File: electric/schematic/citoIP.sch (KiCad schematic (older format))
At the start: 31 parts

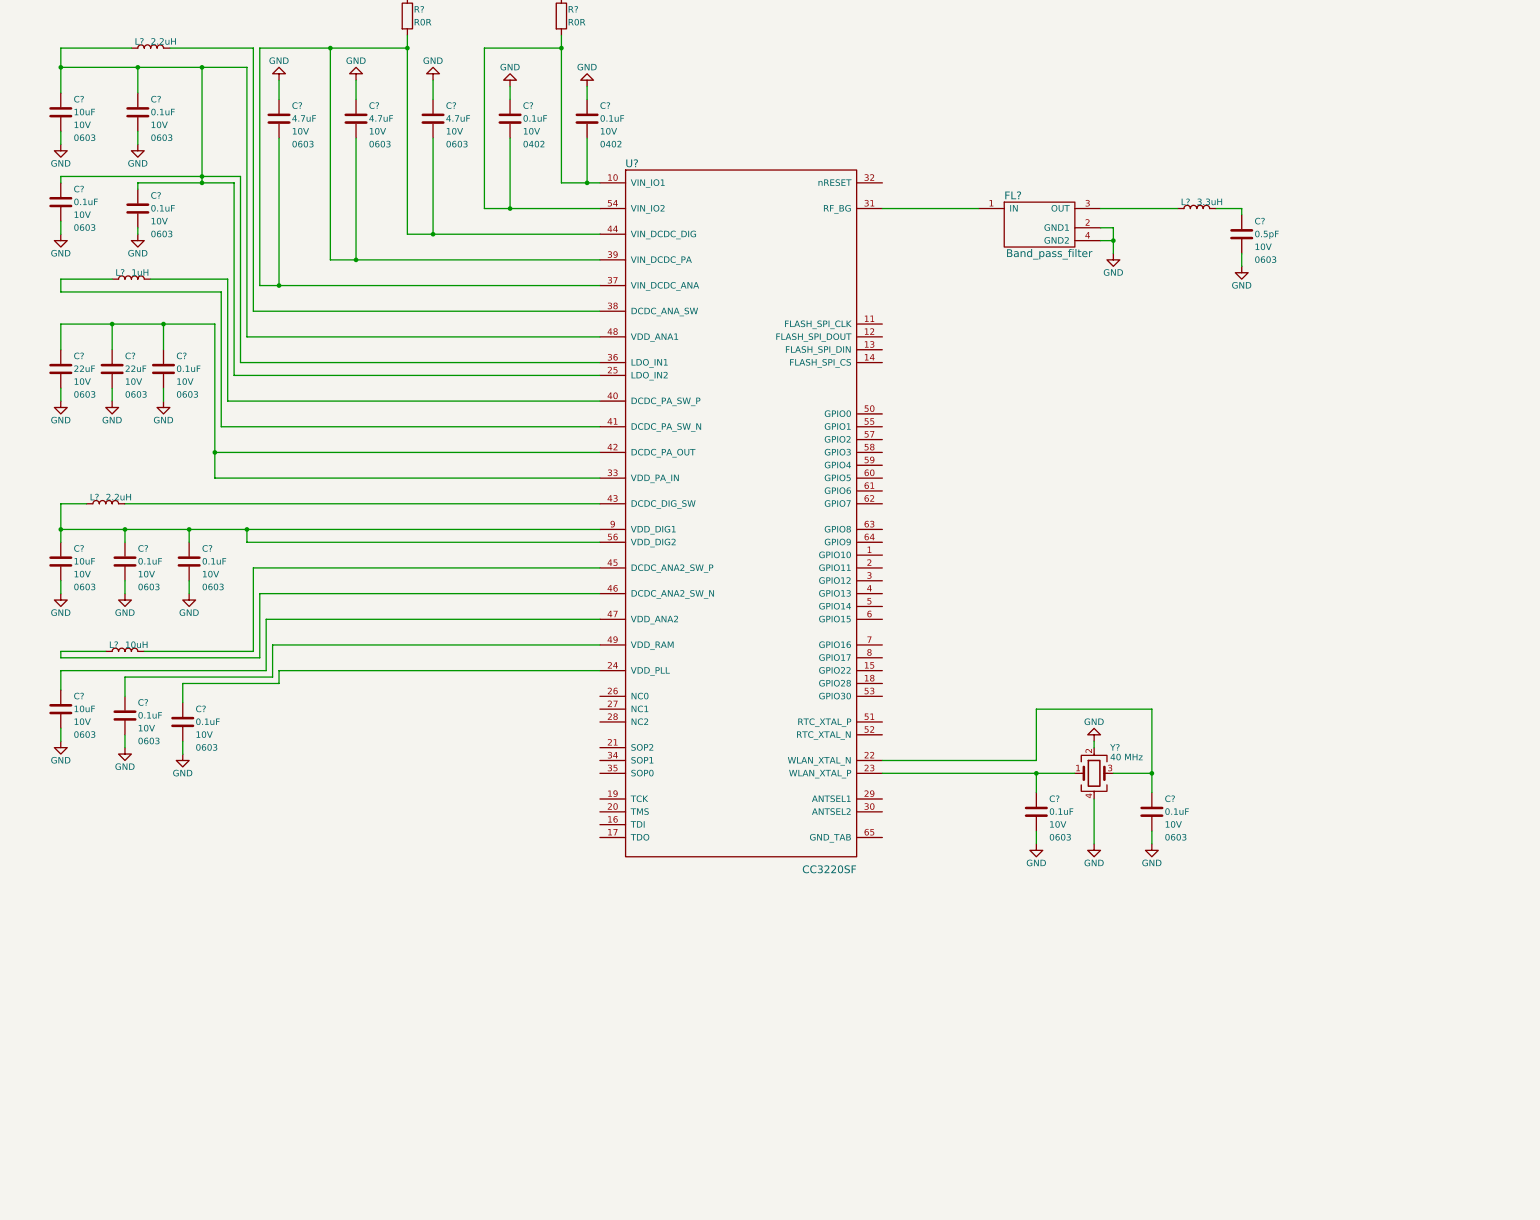
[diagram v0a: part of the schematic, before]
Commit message: Schematic: JTAG, SOP and chip antenna
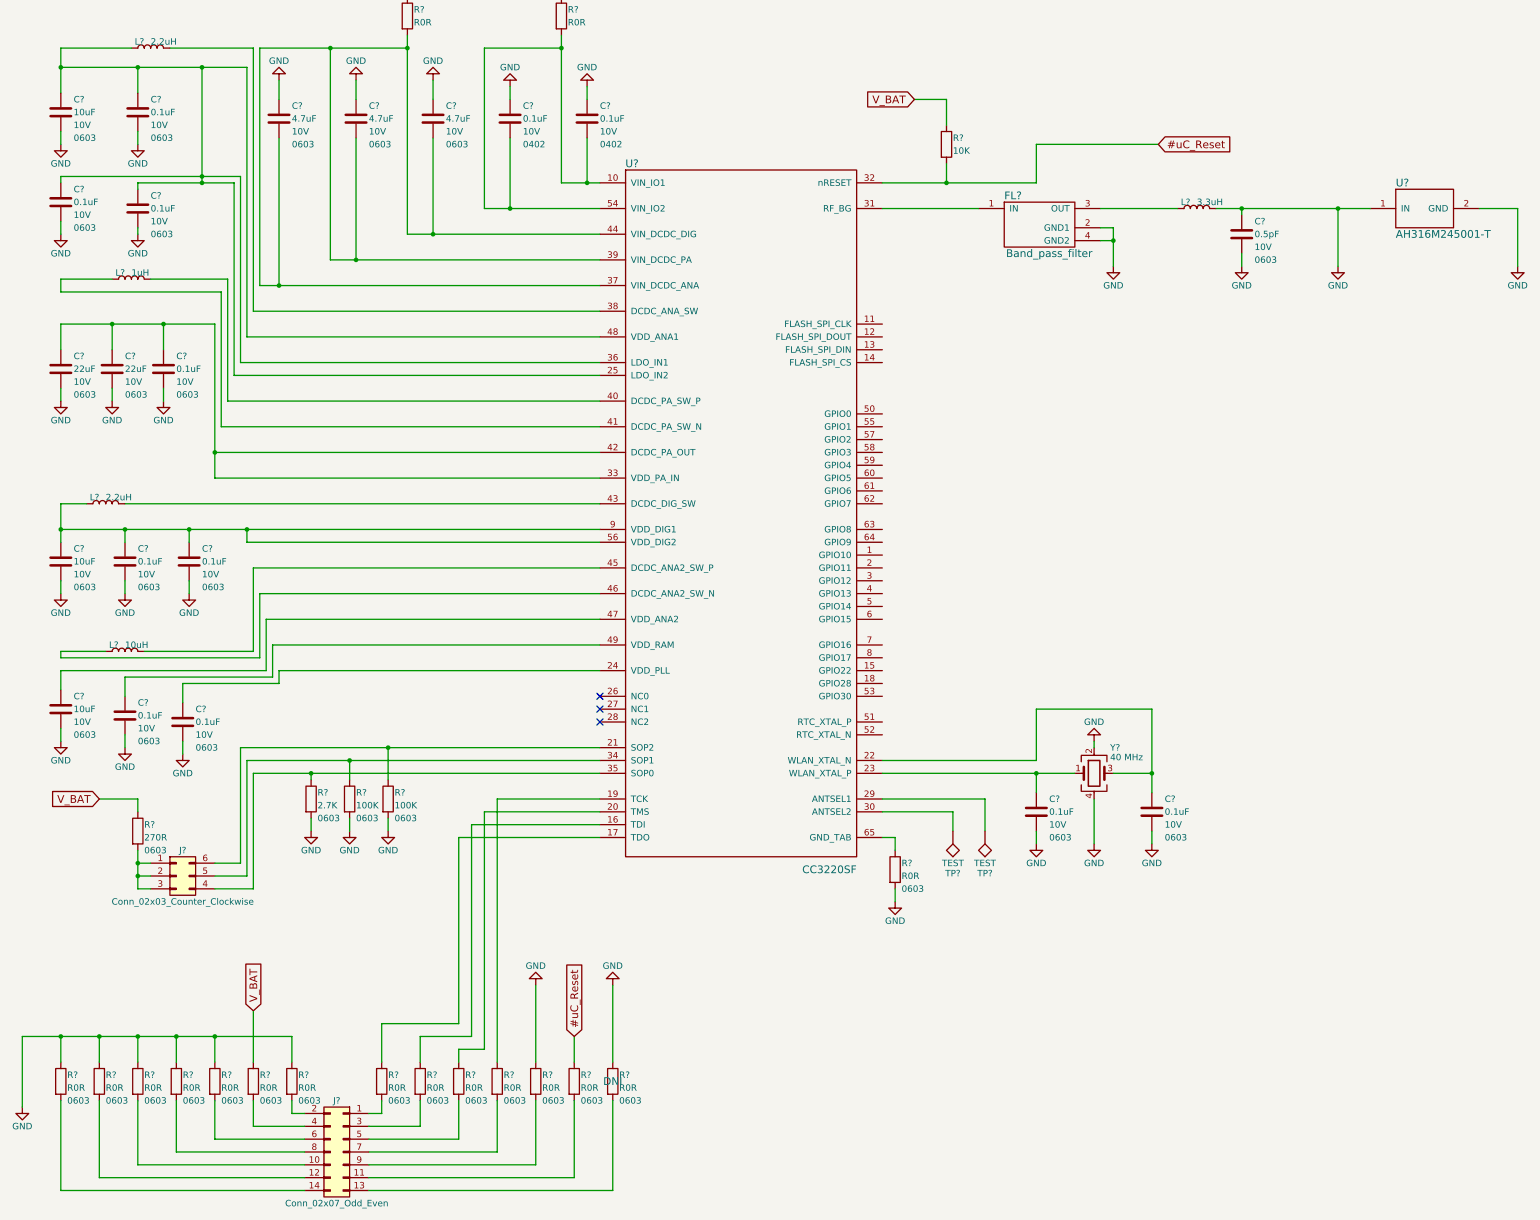
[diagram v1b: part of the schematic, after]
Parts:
- added J?: Conn_02x03_Counter_Clockwise, symbol Conn_02x03_Counter_Clockwise
- added J?: Conn_02x07_Odd_Even, symbol Conn_02x07_Odd_Even
- added R? (x15): R0R, symbol R
- added R?: 2.7K, symbol R
- added R? (x2): 100K, symbol R
- added R?: 270R, symbol R
- added R?: 10K, symbol R
- added TP? (x2): TEST, symbol TEST
- added U?: AH316M245001-T, symbol AH316M245001-T
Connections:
- net GND: now also C?.1, L?.2, R?.1, R?.1, R?.1, R?.1, R?.1, R?.1, R?.1, R?.1, R?.2, R?.2, R?.2, R?.2, U?.1 (IN), U?.2 (GND)
- net V_BAT: now also R?.1, R?.1, R?.1
- net at U?.16 (TDI): now also R?.1
- net at U?.17 (TDO): now also R?.1
- net at U?.19 (TCK): now also R?.1
- net at U?.20 (TMS): now also R?.1
- net at U?.21 (SOP2): now also J?.6 (Pin_6), R?.1
- net at U?.29 (ANTSEL1): now also TP?.1
- net at U?.30 (ANTSEL2): now also TP?.1
- net #uC_Reset: now reaches U?.32 (nRESET)
- net #uC_Reset: now also R?.1, R?.2
- net at U?.34 (SOP1): now also J?.5 (Pin_5), R?.1
- net at U?.35 (SOP0): now also J?.4 (Pin_4), R?.1
- net at U?.65 (GND_TAB): now also R?.1
- new net: J?.1 (Pin_1), J?.2 (Pin_2), J?.3 (Pin_3), R?.2
- new net: J?.1 (Pin_1), R?.2
- new net: J?.10 (Pin_10), R?.2
- new net: J?.11 (Pin_11), R?.2
- new net: J?.12 (Pin_12), R?.2
- new net: J?.13 (Pin_13), R?.2
- new net: J?.14 (Pin_14), R?.2
- new net: J?.2 (Pin_2), R?.2
- new net: J?.3 (Pin_3), R?.2
- new net: J?.4 (Pin_4), R?.2
- new net: J?.5 (Pin_5), R?.2
- new net: J?.6 (Pin_6), R?.2
- new net: J?.7 (Pin_7), R?.2
- new net: J?.8 (Pin_8), R?.2
- new net: J?.9 (Pin_9), R?.2
- no-connect marks 0 -> 3

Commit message: Schematic: CC3220 external flash
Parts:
- added C?: 0.1uF, symbol C
- added R? (x6): R0R, symbol R
- added TP? (x17): TEST, symbol TEST
- added U?: MX25R3235FM1IL0, symbol MX25R3235FM1IL0
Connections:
- net GND: now also C?.2, U?.4 (GND)
- net at U?.11 (FLASH_SPI_CLK): now also R?.2
- net at U?.12 (FLASH_SPI_DOUT): now also R?.2
- net at U?.13 (FLASH_SPI_DIN): now also R?.2
- net at U?.14 (FLASH_SPI_CS): now also R?.2
- net at J?.6 (Pin_6), R?.1, U?.21 (SOP2): now also TP?.1
- net at J?.5 (Pin_5), R?.1, U?.34 (SOP1): now also TP?.1
- net at J?.4 (Pin_4), R?.1, U?.35 (SOP0): now also TP?.1
- net at J?.1 (Pin_1), J?.2 (Pin_2), J?.3 (Pin_3): now also R?.1; no longer R?.2
- net at J?.1 (Pin_1), R?.2: now also TP?.1
- net at J?.10 (Pin_10), R?.2: now also TP?.1
- net at J?.11 (Pin_11), R?.2: now also TP?.1
- net at J?.12 (Pin_12), R?.2: now also TP?.1
- net at J?.13 (Pin_13), R?.2: now also TP?.1
- net at J?.14 (Pin_14), R?.2: now also TP?.1
- net at J?.2 (Pin_2), R?.2: now also TP?.1
- net at J?.3 (Pin_3), R?.2: now also TP?.1
- net at J?.4 (Pin_4), R?.2: now also TP?.1
- net at J?.5 (Pin_5), R?.2: now also TP?.1
- net at J?.6 (Pin_6), R?.2: now also TP?.1
- net at J?.7 (Pin_7), R?.2: now also TP?.1
- net at J?.8 (Pin_8), R?.2: now also TP?.1
- net at J?.9 (Pin_9), R?.2: now also TP?.1
- net V_BAT renamed Radio_VCC
- net Radio_VCC: now also R?.2, R?.1, R?.2; no longer R?.1
- new net: R?.1, U?.1 (#CS)
- new net: R?.1, U?.2 (SO/SIO1)
- new net: C?.1, R?.2, U?.3 (#WP/SIO2), U?.7 (#RESET/SIO3), U?.8 (VCC)
- new net: R?.1, U?.5 (SI/SIO0)
- new net: R?.1, U?.6 (SLCK)
- new net Radio_VCC_from_power: R?.1
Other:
- moved on the sheet: C?, FL?, J?, L?, R?, TP?, U?, Y?

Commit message: Sheet for codec added
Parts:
- removed C? (x13): 0.1uF, symbol C
- removed C? (x3): 4.7uF, symbol C
- removed C? (x3): 10uF, symbol C
- removed C? (x2): 22uF, symbol C
- removed C?: 0.5pF, symbol C
- removed FL?: Band_pass_filter, symbol Band_pass_filter
- removed J?: Conn_02x03_Counter_Clockwise, symbol Conn_02x03_Counter_Clockwise
- removed J?: Conn_02x07_Odd_Even, symbol Conn_02x07_Odd_Even
- removed L? (x2): 2.2uH, symbol L
- removed L?: 1uH, symbol L
- removed L?: 10uH, symbol L
- removed L?: 3.3uH, symbol L
- removed R? (x23): R0R, symbol R
- removed R?: 2.7K, symbol R
- removed R? (x2): 100K, symbol R
- removed R?: 270R, symbol R
- removed R?: 10K, symbol R
- removed TP? (x19): TEST, symbol TEST
- removed U?: CC3220SF, symbol CC3220SF
- removed U?: AH316M245001-T, symbol AH316M245001-T
- removed U?: MX25R3235FM1IL0, symbol MX25R3235FM1IL0
- removed Y?: 40 MHz, symbol Crystal_GND24
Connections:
- no-connect marks 3 -> 0

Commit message: Touch part started
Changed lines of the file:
@@
 $Descr A3 16535 11693
 encoding utf-8
-Sheet 1 3
+Sheet 1 4
 Title "Wi-fi"
 Date ""
@@
 F1 "radio_sheet.sch" 60
 $EndSheet
+$Sheet
+S 3900 700  1400 1300
+U 5AC8DE19
+F0 "Sheet5AC8DE18" 60
+F1 "touch_sheet.sch" 60
+$EndSheet
 $EndSCHEMATC
